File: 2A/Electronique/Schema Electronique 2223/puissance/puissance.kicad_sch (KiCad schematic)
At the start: 28 parts, among them J101 Bat 2, J102 Bat 1, J103 AU, J104 Switch, J105 Conn_01x03, J107 Conn_01x02, J108 Conn_01x02, J109 Conn_01x02, J110 Conn_01x02, J111 Conn_01x02, J112 Conn_01x04, J113 Conn_02x20_Odd_Even, U101 74LVC2G241

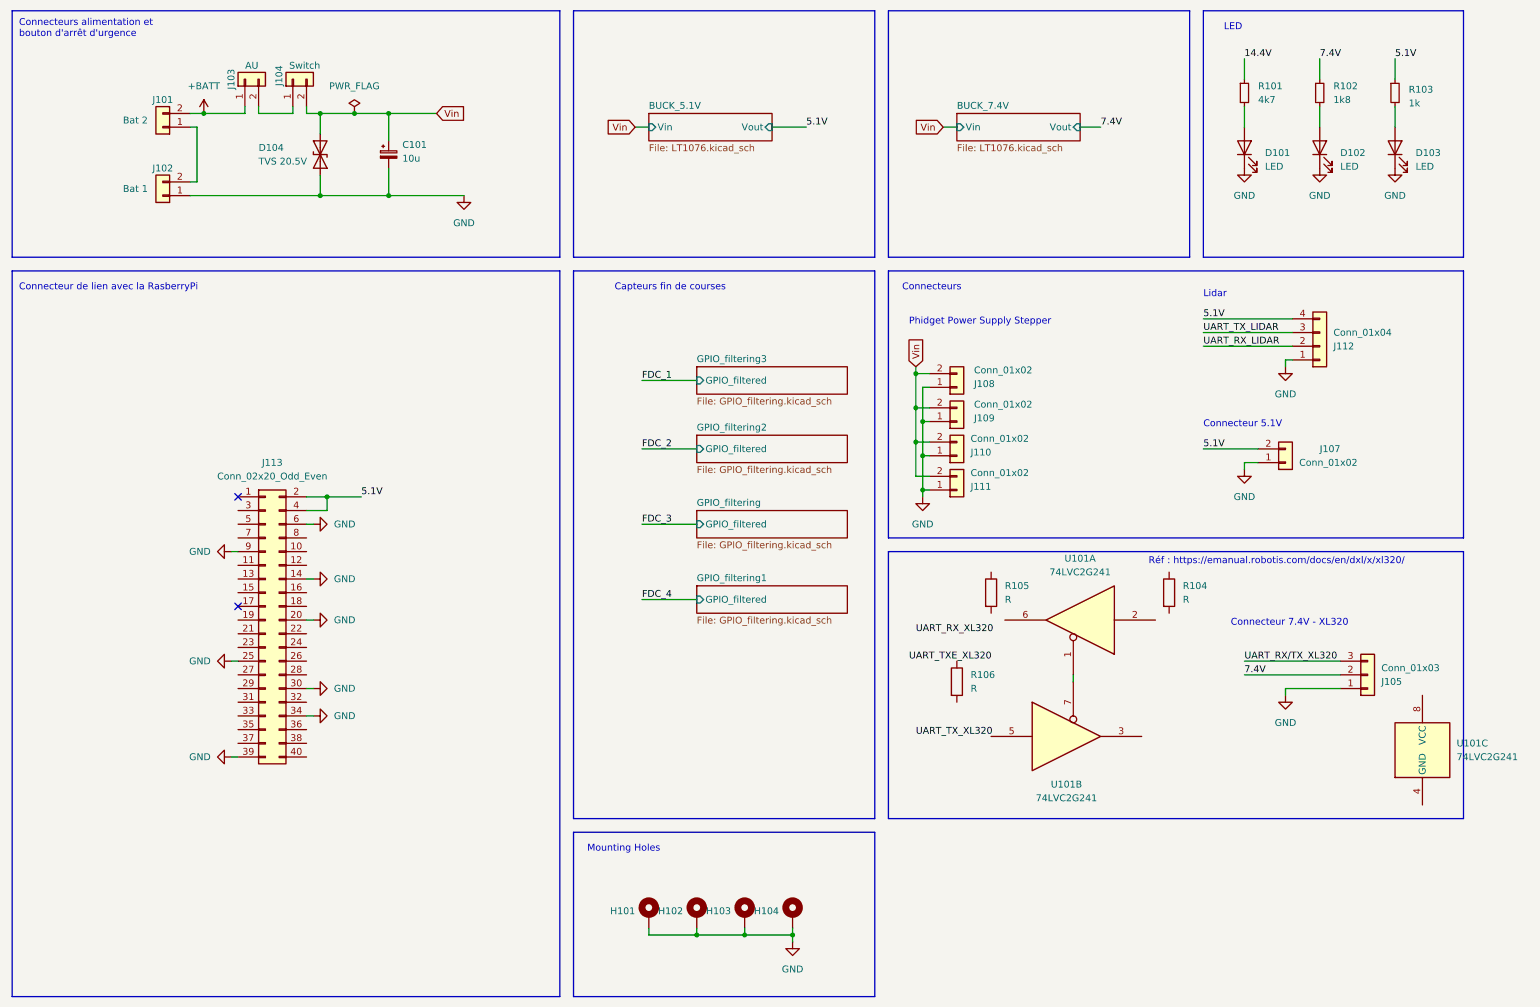
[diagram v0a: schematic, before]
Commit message: suppression diode et changement des feuille hiérarchique
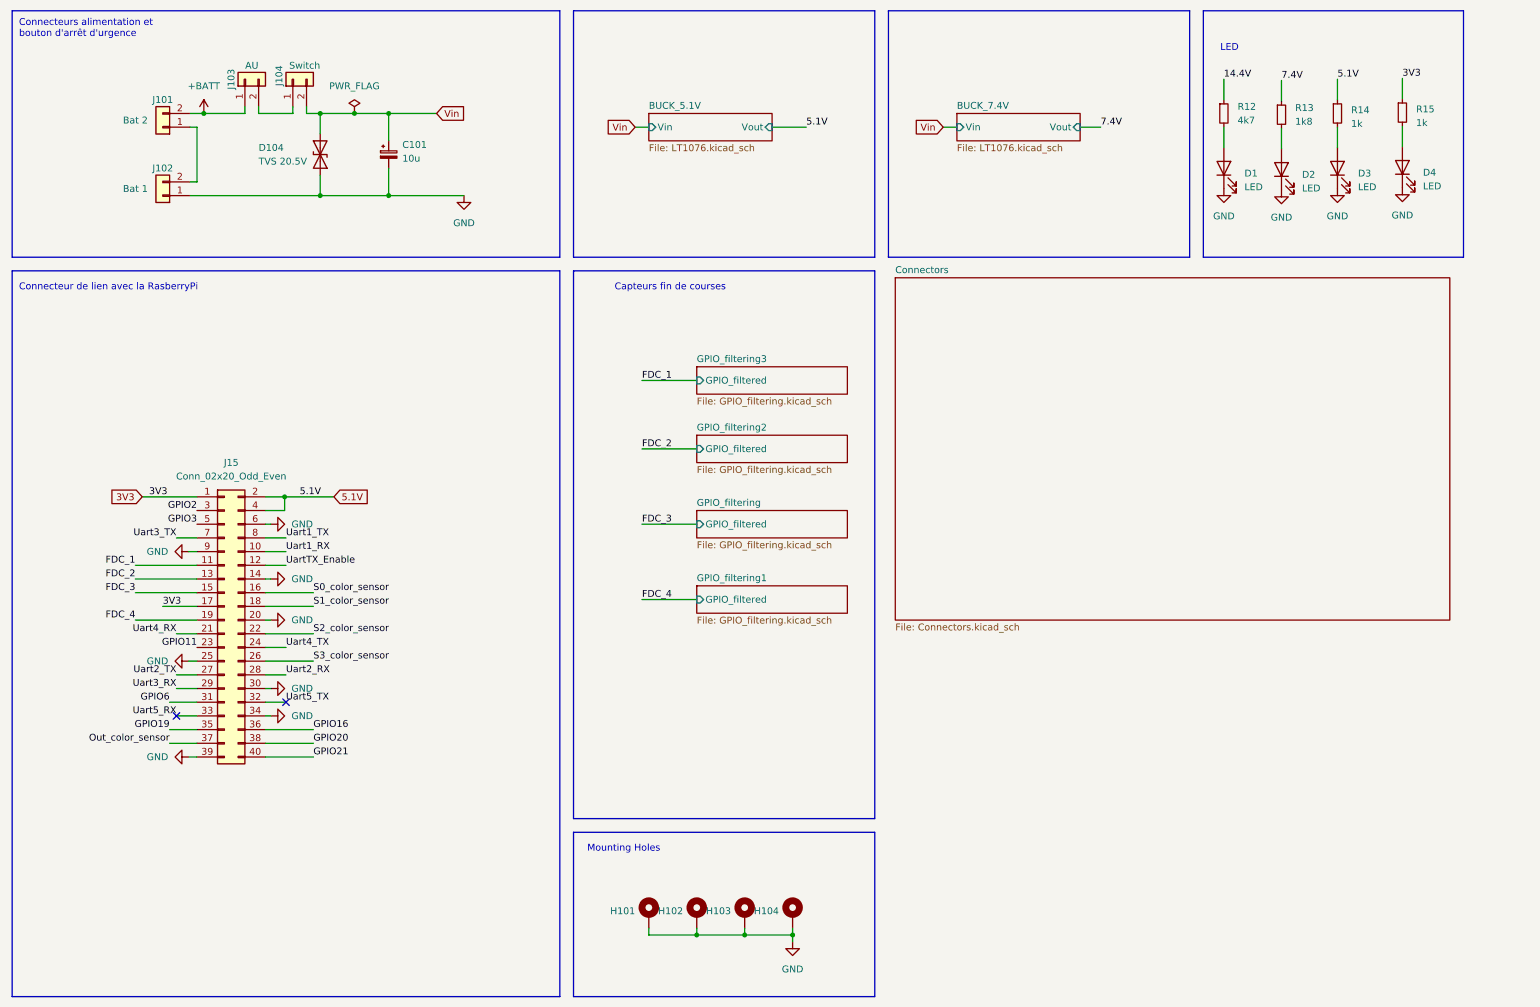
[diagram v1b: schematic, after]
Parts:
- removed D101, D102, D103: LED, LED_SMD:LED_0603_1608Metric_Pad1.05x0.95mm_HandSolder, symbol Device:LED
- removed J105: Conn_01x03, symbol Connector_Generic:Conn_01x03
- removed J107, J108, J109, J110, J111: Conn_01x02, symbol Connector_Generic:Conn_01x02
- removed J112: Conn_01x04, symbol Connector_Generic:Conn_01x04
- removed J113: Conn_02x20_Odd_Even, symbol Connector_Generic:Conn_02x20_Odd_Even
- removed R101: 4k7, Resistor_SMD:R_0603_1608Metric_Pad0.98x0.95mm_HandSolder, symbol Device:R_Small
- removed R102: 1k8, Resistor_SMD:R_0603_1608Metric_Pad0.98x0.95mm_HandSolder, symbol Device:R_Small
- removed R103: 1k, Resistor_SMD:R_0603_1608Metric_Pad0.98x0.95mm_HandSolder, symbol Device:R_Small
- removed R104, R105, R106: R, symbol Device:R
- removed U101: 74LVC2G241, symbol 74xGxx:74LVC2G241
- added D1, D2, D3, D4: LED, LED_SMD:LED_0603_1608Metric_Pad1.05x0.95mm_HandSolder, symbol Device:LED
- added J15: Conn_02x20_Odd_Even, symbol Connector_Generic:Conn_02x20_Odd_Even
- added R12: 4k7, Resistor_SMD:R_0603_1608Metric_Pad0.98x0.95mm_HandSolder, symbol Device:R_Small
- added R13: 1k8, Resistor_SMD:R_0603_1608Metric_Pad0.98x0.95mm_HandSolder, symbol Device:R_Small
- added R14, R15: 1k, Resistor_SMD:R_0603_1608Metric_Pad0.98x0.95mm_HandSolder, symbol Device:R_Small
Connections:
- net 14.4V: now also R12.1
- net 5.1V: now also J15.2 (Pin_2), J15.4 (Pin_4), R14.1
- net 7.4V: now also R13.1
- net FDC_1: now also J15.11 (Pin_11)
- net FDC_2: now also J15.13 (Pin_13)
- net FDC_3: now also J15.15 (Pin_15)
- net FDC_4: now also J15.19 (Pin_19)
- net GND: now also D1.1 (K), D2.1 (K), D3.1 (K), D4.1 (K), J15.14 (Pin_14), J15.20 (Pin_20), J15.25 (Pin_25), J15.30 (Pin_30), J15.34 (Pin_34), J15.39 (Pin_39), J15.6 (Pin_6), J15.9 (Pin_9)
- new net: D1.2 (A), R12.2
- new net: D3.2 (A), R14.2
- new net: D2.2 (A), R13.2
- new net: D4.2 (A), R15.2
- new net 3V3: J15.1 (Pin_1), J15.17 (Pin_17), R15.1
- new net GPIO11: J15.23 (Pin_23)
- new net GPIO16: J15.36 (Pin_36)
- new net GPIO19: J15.35 (Pin_35)
- new net GPIO2: J15.3 (Pin_3)
- new net GPIO20: J15.38 (Pin_38)
- new net GPIO21: J15.40 (Pin_40)
- new net GPIO3: J15.5 (Pin_5)
- new net GPIO6: J15.31 (Pin_31)
- new net Out_color_sensor: J15.37 (Pin_37)
- new net S0_color_sensor: J15.16 (Pin_16)
- new net S1_color_sensor: J15.18 (Pin_18)
- new net S2_color_sensor: J15.22 (Pin_22)
- new net S3_color_sensor: J15.26 (Pin_26)
- new net Uart1_RX: J15.10 (Pin_10)
- new net Uart1_TX: J15.8 (Pin_8)
- new net Uart2_RX: J15.28 (Pin_28)
- new net Uart2_TX: J15.27 (Pin_27)
- new net Uart3_RX: J15.29 (Pin_29)
- new net Uart3_TX: J15.7 (Pin_7)
- new net Uart4_RX: J15.21 (Pin_21)
- new net Uart4_TX: J15.24 (Pin_24)
- new net Uart5_RX: J15.33 (Pin_33)
- new net Uart5_TX: J15.32 (Pin_32)
- new net UartTX_Enable: J15.12 (Pin_12)
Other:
- added sheet Connectors (Connectors.kicad_sch)
- note removed: "Connecteur 5.1V"
- note removed: "Connecteur 7.4V - XL320"
- note removed: "Connecteurs"
- note removed: "Lidar"
- note removed: "Phidget Power Supply Stepper"
- note removed: "Réf : https://emanual.robotis.com/docs/en/dxl/x/xl320/"

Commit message: update puissance
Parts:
- removed C101: 10u, Capacitor_SMD:CP_Elec_5x5.4, symbol Device:C_Polarized_Small
- removed D1: LED, LED_SMD:LED_0603_1608Metric_Pad1.05x0.95mm_HandSolder, symbol Device:LED
- removed D104: TVS 20.5V, symbol Diode:1.5KExxCA
- removed H101, H102, H103, H104: MountingHole_Pad, MountingHole:MountingHole_3.2mm_M3_Pad_Via, symbol Mechanical:MountingHole_Pad
- removed J101: Bat 2, symbol Connector_Generic:Conn_01x02
- removed J102: Bat 1, symbol Connector_Generic:Conn_01x02
- removed J103: AU, symbol Connector_Generic:Conn_01x02
- removed J104: Switch, symbol Connector_Generic:Conn_01x02
- removed J15: Conn_02x20_Odd_Even, symbol Connector_Generic:Conn_02x20_Odd_Even
- removed R12: 4k7, Resistor_SMD:R_0603_1608Metric_Pad0.98x0.95mm_HandSolder, symbol Device:R_Small
- removed R13: 1k8, Resistor_SMD:R_0603_1608Metric_Pad0.98x0.95mm_HandSolder, symbol Device:R_Small
- removed R14, R15: 1k, Resistor_SMD:R_0603_1608Metric_Pad0.98x0.95mm_HandSolder, symbol Device:R_Small
- added C1: 10u, Capacitor_SMD:CP_Elec_4x5.4, symbol Device:C_Polarized_Small
- added D1: TVS 20.5V, Diode_SMD:D_SMB, symbol Diode:1.5KExxCA
- added D5: LED, LED_SMD:LED_0603_1608Metric, symbol Device:LED
- added H1, H2, H3, H4: MountingHole_Pad, MountingHole:MountingHole_2.7mm_M2.5_Pad_Via, symbol Mechanical:MountingHole_Pad
- added J1: Bat 2, custom:691322110002, symbol Connector_Generic:Conn_01x02
- added J10: Conn_01x02, Connector_JST:JST_XH_B2B-XH-A_1x02_P2.50mm_Vertical, symbol Connector_Generic:Conn_01x02
- added J11: Conn_GND, Connector_PinHeader_2.54mm:PinHeader_1x08_P2.54mm_Vertical, symbol Connector_Generic:Conn_01x08
- added J12: Conn_GPIO_unused, Connector_PinHeader_2.54mm:PinHeader_1x08_P2.54mm_Vertical, symbol Connector_Generic:Conn_01x08
- added J13: Conn_3.3V, Connector_PinHeader_2.54mm:PinHeader_1x08_P2.54mm_Vertical, symbol Connector_Generic:Conn_01x08
- added J14, J15: Conn_01x05, Connector_JST:JST_XH_B5B-XH-A_1x05_P2.50mm_Vertical, symbol Connector_Generic:Conn_01x05
- added J2: Bat 1, custom:691322110002, symbol Connector_Generic:Conn_01x02
- added J3: AU, custom:691322110002, symbol Connector_Generic:Conn_01x02
- added J4: Switch, custom:691322110002, symbol Connector_Generic:Conn_01x02
- added J5: Conn_RPI, Connector_PinSocket_2.54mm:PinSocket_2x20_P2.54mm_Vertical, symbol Connector_Generic:Conn_02x20_Odd_Even
- added J6: Conn_Phidget_PS_Stepper_1, Connector_JST:JST_XH_B2B-XH-A_1x02_P2.50mm_Vertical, symbol Connector_Generic:Conn_01x02
- added J7: Conn_Phidget_PS_Stepper_2, Connector_JST:JST_XH_B2B-XH-A_1x02_P2.50mm_Vertical, symbol Connector_Generic:Conn_01x02
- added J8: Conn_Phidget_PS_Stepper_3, Connector_JST:JST_XH_B2B-XH-A_1x02_P2.50mm_Vertical, symbol Connector_Generic:Conn_01x02
- added J9: Conn_Phidget_PS_Stepper_4, Connector_JST:JST_XH_B2B-XH-A_1x02_P2.50mm_Vertical, symbol Connector_Generic:Conn_01x02
- added R1: 4k7, Resistor_SMD:R_0402_1005Metric, symbol Device:R_Small
- added R2: 1k8, Resistor_SMD:R_0402_1005Metric, symbol Device:R_Small
- added R3, R4: 1k, Resistor_SMD:R_0402_1005Metric, symbol Device:R_Small
- added TP1: TestPoint, Connector_Pin:Pin_D0.9mm_L10.0mm_W2.4mm_FlatFork, symbol Connector:TestPoint
- added TP2: 5.1V, Connector_Pin:Pin_D0.9mm_L10.0mm_W2.4mm_FlatFork, symbol Connector:TestPoint
- added TP3: 7.4V, Connector_Pin:Pin_D0.9mm_L10.0mm_W2.4mm_FlatFork, symbol Connector:TestPoint
- added TP4: 3V3, Connector_Pin:Pin_D0.9mm_L10.0mm_W2.4mm_FlatFork, symbol Connector:TestPoint
- D2, D3, D4: footprint LED_SMD:LED_0603_1608Metric_Pad1.05x0.95mm_HandSolder -> LED_SMD:LED_0603_1608Metric
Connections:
- net 14.4V: now also R1.1
- net 3V3: now also J14.1 (Pin_1)
- net 5.1V: now also J10.2 (Pin_2), J5.2 (Pin_2), J5.4 (Pin_4), R3.1, TP2.1
- net 7.4V: now also R2.1, TP3.1
- net FDC_1: now also J5.11 (Pin_11)
- net FDC_2: now also J5.13 (Pin_13)
- net FDC_3: now also J5.15 (Pin_15)
- net FDC_4: now also J5.19 (Pin_19)
- net GND: now also C1.2, D1.2 (A2), D5.1 (K), H1.1, H2.1, H3.1, H4.1, J10.1 (Pin_1), J11.1 (Pin_1), J11.2 (Pin_2), J11.3 (Pin_3), J11.4 (Pin_4), J11.5 (Pin_5), J11.6 (Pin_6), J11.7 (Pin_7), J11.8 (Pin_8), J14.2 (Pin_2), J14.3 (Pin_3), J14.5 (Pin_5), J2.1 (Pin_1), J5.14 (Pin_14), J5.20 (Pin_20), J5.25 (Pin_25), J5.30 (Pin_30), J5.34 (Pin_34), J5.39 (Pin_39), J5.6 (Pin_6), J5.9 (Pin_9), J6.1 (Pin_1), J7.1 (Pin_1), J8.1 (Pin_1), J9.1 (Pin_1)
- net GPIO11: now also J12.4 (Pin_4), J5.23 (Pin_23)
- net GPIO16: now also J12.5 (Pin_5), J5.36 (Pin_36)
- net GPIO19: now also J12.6 (Pin_6), J5.35 (Pin_35)
- net GPIO2: now also J12.1 (Pin_1), J5.3 (Pin_3)
- net GPIO20: now also J12.7 (Pin_7), J5.38 (Pin_38)
- net GPIO21: now also J12.8 (Pin_8), J5.40 (Pin_40)
- net GPIO3: now also J12.2 (Pin_2), J5.5 (Pin_5)
- net GPIO6: now also J12.3 (Pin_3), J5.31 (Pin_31)
- net Out_color_sensor: now also J15.1 (Pin_1), J5.37 (Pin_37)
- net S0_color_sensor: now also J15.5 (Pin_5), J5.16 (Pin_16)
- net S1_color_sensor: now also J15.4 (Pin_4), J5.18 (Pin_18)
- net S2_color_sensor: now also J15.3 (Pin_3), J5.22 (Pin_22)
- net S3_color_sensor: now also J15.2 (Pin_2), J5.26 (Pin_26)
- net Uart1_RX: now also J5.10 (Pin_10)
- net Uart1_TX: now also J5.8 (Pin_8)
- net Uart2_RX: now also J5.28 (Pin_28)
- net Uart2_TX: now also J5.27 (Pin_27)
- net Uart3_RX: now also J5.29 (Pin_29)
- net Uart3_TX: now also J5.7 (Pin_7)
- net Uart4_RX: now also J5.21 (Pin_21)
- net Uart4_TX: now also J5.24 (Pin_24)
- net Uart5_RX: now also J5.33 (Pin_33)
- net Uart5_TX: now also J5.32 (Pin_32)
- net UartTX_Enable: now also J5.12 (Pin_12)
- net Vin: now also C1.1, D1.1 (A1), J4.2 (Pin_2), J6.2 (Pin_2), J7.2 (Pin_2), J8.2 (Pin_2), J9.2 (Pin_2), TP1.1
- net at D3.2 (A): now also R2.2
- net at D2.2 (A): now also R1.2
- net at D4.2 (A): now also R3.2
- new net: J3.2 (Pin_2), J4.1 (Pin_1)
- new net: D5.2 (A), R4.2
- new net: J1.1 (Pin_1), J2.2 (Pin_2)
- new net +3.3V: J13.1 (Pin_1), J13.2 (Pin_2), J13.3 (Pin_3), J13.4 (Pin_4), J13.5 (Pin_5), J13.6 (Pin_6), J13.7 (Pin_7), J13.8 (Pin_8), J5.1 (Pin_1), J5.17 (Pin_17), R4.1, TP4.1
- new net 5V: J14.4 (Pin_4)
- new net V_BAT: J1.2 (Pin_2), J3.1 (Pin_1)
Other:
- removed sheet Connectors
- added sheet IHM_Connector (UART_Connector.kicad_sch)
- added sheet LIDAR_Connector (UART_Connector.kicad_sch)
- added sheet UART4_Connector1 (UART_Connector.kicad_sch)
- added sheet XL_320_connector_and_buffer (XL320.kicad_sch)
- sheet GPIO_filtering ports: added PWR; removed none
- sheet GPIO_filtering1 ports: added PWR; removed none
- sheet GPIO_filtering2 ports: added PWR; removed none
- sheet GPIO_filtering3 ports: added PWR; removed none
- note added: "Color Sensor TCS230"
- note added: "Connecteur 5.1V"
- note added: "GPIO unused"
- note added: "Phidget Power Supply Stepper"
- note added: "UART"
